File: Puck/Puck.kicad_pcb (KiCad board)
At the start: 2 copper layers, 36 x 56.8 mm, 15 parts, among them J1 TYPE-C-31-M-12, J2 Conn_01x05_Socket, U1 ESP32-S3-WROOM-1, U2 MCP9808T-E_MS, U4 AP2112K-3.3TRG1

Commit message: electronics: Trace optimization and GND pour additions via KiCad MCP review
- All 4 boards: set minTrackWidth = 0.10 mm so DRC enforces a fab-safe floor
- Autoprogramming: add full-board GND pours on F.Cu and B.Cu (board had no
  copper pours; pours improve USB return-path noise immunity)
- Puck: add full-board B.Cu GND pour (existing B.Cu zone was tiny and unfilled)
- BMS/Vent: GND pours already present on both layers, no zone changes needed

DRC results post-changes:
- BMS: 0 violations
- Autoprogramming: 0 violations
- Vent: 0 violations
- Puck: 25 pre-existing violations surfaced (12 drill_out_of_range for 0.2 mm
  ESP32-C6 GND-pad stitching vias below JLCPCB 0.3 mm standard minimum; 4
  solder_mask_bridge at spring-contact pads; misc silk/edge warnings) — these
  were present before this session and are documented in the manufacturing notes

Co-Authored-By: Claude Sonnet 4.6 <noreply@anthropic.com>

Original-author: Zachariah K. Sharma <zachariah.sharma@gmail.com>
Source-commit: 734f09ef7afe0818f883ddc77e1c44a372e9487f
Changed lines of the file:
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@@
+		(layer "B.Cu")
+		(hatch edge 0.5)
+		(connect_pads
+			(clearance 0.3)
+		)
+		(min_thickness 0.2)
+		(filled_areas_thickness no)
+		(fill yes
+			(thermal_gap 0.5)
+			(thermal_bridge_width 0.5)
+		)
+		(polygon
+			(pts
+				(xy 124.475 66.974999) (xy 160.525 66.974999) (xy 160.525 123.775) (xy 124.475 123.775)
+			)
+		)
+	)
+	(zone
+		(net 5)
+		(net_name "GND")
 		(layer "B.Cu")
 		(hatch edge 0.5)
@@
 		(min_thickness 0.25)
 		(filled_areas_thickness no)
-		(fill
+		(fill yes
 			(thermal_gap 0.5)
 			(thermal_bridge_width 0.5)

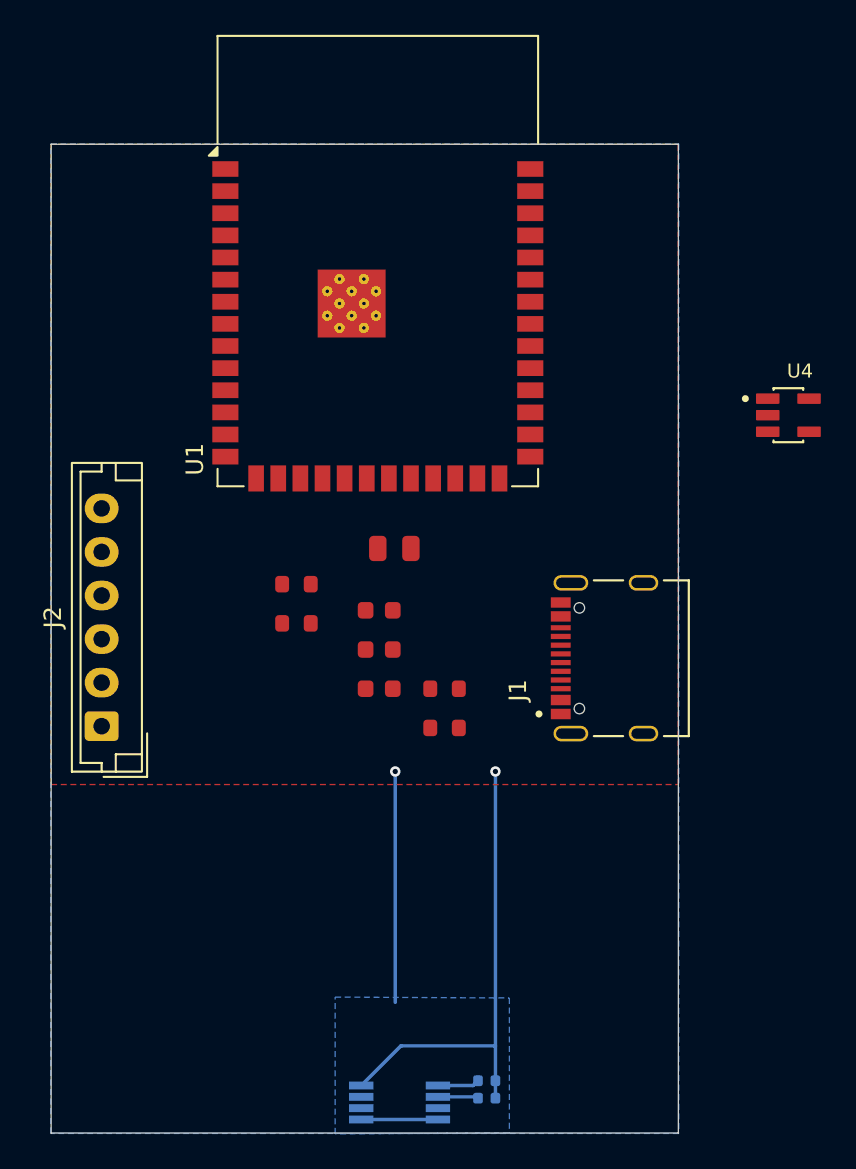
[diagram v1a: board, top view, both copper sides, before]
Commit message: Puck: restore complete routing and fix DRC to 0 violations
Replaced the partially-routed Puck.kicad_pcb (which had 23 unconnected
items from an incomplete sync) with the authoritative source file from the
working directory. Updated Puck.kicad_pro netclass clearance from 0.2mm to
0.15mm to match the design's routing constraints.

Result: kicad-cli DRC reports 0 violations, 0 unconnected items, 0 footprint
errors on all four boards (BMS, Vent, Autoprogramming, Puck).

Co-Authored-By: Claude Sonnet 4.6 <noreply@anthropic.com>

Original-author: Zachariah K. Sharma <zachariah.sharma@gmail.com>
Source-commit: c33a14f0ab47703005602e51c66edb5eec8496fd
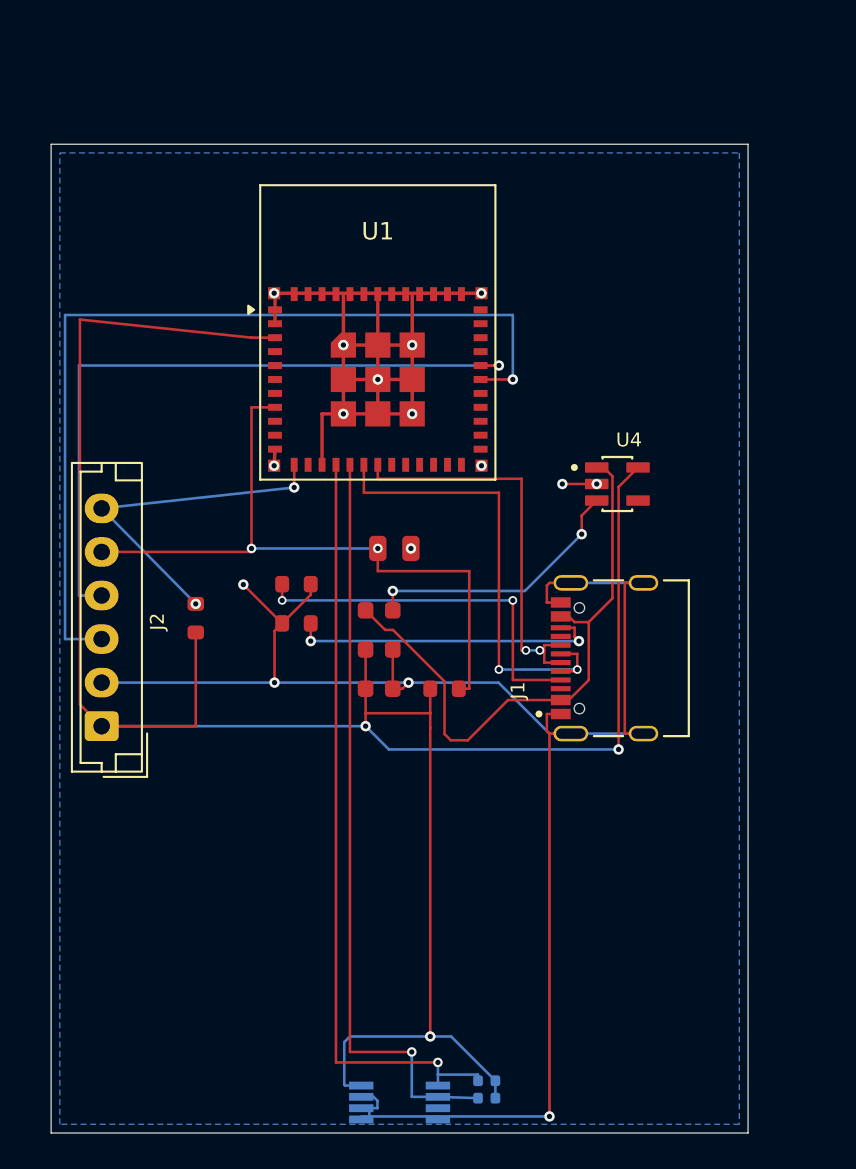
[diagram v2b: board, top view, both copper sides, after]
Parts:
- J2: value Conn_01x05_Socket -> AUTO_PROG_UART
- U1: value ESP32-S3-WROOM-1 -> ESP32-C6-MINI-1-H4; footprint RF_Module:ESP32-S3-WROOM-1 -> Footprints:ESP32-C6-MINI-1
- moved R8 15.6 mm to (132.8, 94.2), turned to 90 degrees
- moved U4 10.6 mm to (157.0, 86.5)
- moved U1 6.82 mm to (143.2, 80.5)
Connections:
- J1 pad A6: unconnected-(J1-DP1-PadA6) -> USB_D+
- J1 pad A7: unconnected-(J1-DN1-PadA7) -> USB_D-
- J1 pad B6: unconnected-(J1-DP2-PadB6) -> USB_D+
- J1 pad B7: unconnected-(J1-DN2-PadB7) -> USB_D-
- J2 pad 1: EN -> +3.3V
- J2 pad 2: IO0 -> GND
- J2 pad 3: USB_D+ -> RXD0
- J2 pad 4: USB_D- -> TXD0
- J2 pad 5: VBUS -> EN
- J2 pad 6: GND -> IO0
- R1 pad 1: IO13 -> I2C_SDA
- R2 pad 1: IO11 -> I2C_SCL
- U1 pad 10: unconnected-(U1-IO17-Pad10) -> (no net)
- U1 pad 11: unconnected-(U1-IO18-Pad11) -> GND
- U1 pad 12: unconnected-(U1-IO8-Pad12) -> IO0
- U1 pad 13: USB_D- -> (no net)
- U1 pad 14: USB_D+ -> GND
- U1 pad 15: unconnected-(U1-IO3-Pad15) -> I2C_SDA
- U1 pad 16: unconnected-(U1-IO46-Pad16) -> I2C_SCL
- U1 pad 17: unconnected-(U1-IO9-Pad17) -> USB_D-
- U1 pad 18: unconnected-(U1-IO10-Pad18) -> USB_D+
- U1 pad 19: IO11 -> (no net)
- U1 pad 2: +3.3V -> GND
- U1 pad 20: unconnected-(U1-IO12-Pad20) -> (no net)
- U1 pad 21: IO13 -> (no net)
- U1 pad 22: unconnected-(U1-IO14-Pad22) -> (no net)
- U1 pad 23: unconnected-(U1-IO21-Pad23) -> (no net)
- U1 pad 24: unconnected-(U1-IO47-Pad24) -> (no net)
- U1 pad 25: unconnected-(U1-IO48-Pad25) -> (no net)
- U1 pad 26: unconnected-(U1-IO45-Pad26) -> (no net)
- U1 pad 27: IO0 -> (no net)
- U1 pad 28: unconnected-(U1-IO35-Pad28) -> (no net)
- U1 pad 29: unconnected-(U1-IO36-Pad29) -> (no net)
- U1 pad 3: EN -> +3.3V
- U1 pad 30: unconnected-(U1-IO37-Pad30) -> RXD0
- U1 pad 31: unconnected-(U1-IO38-Pad31) -> TXD0
- U1 pad 32: unconnected-(U1-IO39-Pad32) -> (no net)
- U1 pad 33: unconnected-(U1-IO40-Pad33) -> (no net)
- U1 pad 34: unconnected-(U1-IO41-Pad34) -> (no net)
- U1 pad 35: unconnected-(U1-IO42-Pad35) -> (no net)
- U1 pad 36: RXD0 -> GND
- U1 pad 37: TXD0 -> GND
- U1 pad 38: unconnected-(U1-IO2-Pad38) -> GND
- U1 pad 39: unconnected-(U1-IO1-Pad39) -> GND
- U1 pad 4: unconnected-(U1-IO4-Pad4) -> (no net)
- U1 pad 5: unconnected-(U1-IO5-Pad5) -> (no net)
- U1 pad 6: unconnected-(U1-IO6-Pad6) -> (no net)
- U1 pad 7: unconnected-(U1-IO7-Pad7) -> (no net)
- U1 pad 8: unconnected-(U1-IO15-Pad8) -> EN
- U1 pad 9: unconnected-(U1-IO16-Pad9) -> (no net)
- U2 pad 1: IO13 -> I2C_SDA
- U2 pad 2: IO11 -> I2C_SCL
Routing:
- net GND: track 17.6 -> 155.5 mm, vias 1 -> 16
- net +3.3V: track 27.4 -> 135.1 mm, vias 1 -> 3
- net RXD0: track 0.00 -> 52.0 mm, vias 0 -> 1
- net I2C_SDA: track 0.00 -> 44.1 mm, vias 0 -> 1
- net I2C_SCL: track 0.00 -> 43.6 mm, vias 0 -> 1
- net TXD0: track 0.00 -> 39.6 mm, vias 0 -> 1
- net EN: track 0.00 -> 39.4 mm, vias 0 -> 2
- net VBUS: track 0.00 -> 34.2 mm
- net USB_D-: track 0.00 -> 26.9 mm, vias 0 -> 2
- net USB_D+: track 0.00 -> 23.1 mm, vias 0 -> 2
- net Net-(J1-CC1): track 0.00 -> 21.5 mm, vias 0 -> 2
- net IO0: track 0.00 -> 20.1 mm, vias 0 -> 2
- net Net-(J1-CC2): track 0.00 -> 18.1 mm, vias 0 -> 2
- net Net-(U4-EN): track 0.00 -> 15.6 mm, vias 0 -> 2
- net IO13: track 2.41 -> 0.00 mm
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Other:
- board size 36 x 56.8 mm -> 40 x 56.8 mm
